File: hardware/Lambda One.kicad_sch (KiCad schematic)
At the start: 7 parts, among them IC1 01, J1 Conn_01x02, SW1 SW_Push, U1 W65C816SxP, U3 ATF22V10C, Y1 TFT680

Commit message: Added Board Register
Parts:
- removed R1: 4.7k, symbol Device:R_Small
- added C1, C20: 1uF, Capacitor_SMD:C_0603_1608Metric, symbol Device:C_Small
- added C21, C23, C25, C26, C27, C30, C4, C5: 100nF, Capacitor_SMD:C_0603_1608Metric, symbol Device:C_Small
- added L1: 120R @ 100MHz, Inductor_SMD:L_0603_1608Metric, symbol Device:L_Ferrite_Small
- added R17: 4.7k, Resistor_SMD:R_0603_1608Metric, symbol Device:R_Small_US
- added TP13: TestPoint_Small, TestPoint:TestPoint_Pad_D1.5mm, symbol Connector:TestPoint_Small
- added U6: 74AHC1G04, Package_TO_SOT_SMD:SOT-23-5, symbol 74xGxx:74AHC1G04
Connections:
- net +5V: now also U3.24 (VCC), R17.2
- net GND: now also C1.2, C20.2, C21.2, C23.2, C25.2, C26.2, C27.2, C30.2, C4.2, C5.2, U6.3 (GND)
- net IRQ_{1}: now also R17.1
- net R/~{W}: now also U6.2
- net BANK_{CS} renamed BoardReg_{~{CS}}
- new net +3.3V: C1.1, C4.1, C5.1, L1.1, U6.5 (VCC)
- new net +3.3VA: C20.1, C21.1, C23.1, C25.1, C26.1, C27.1, C30.1, L1.2, TP13.1
- new net ~{R}/W: U6.4
- no-connect marks 17 -> 16
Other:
- moved on the sheet: IC1, J1, SW1, U1, U3, Y1

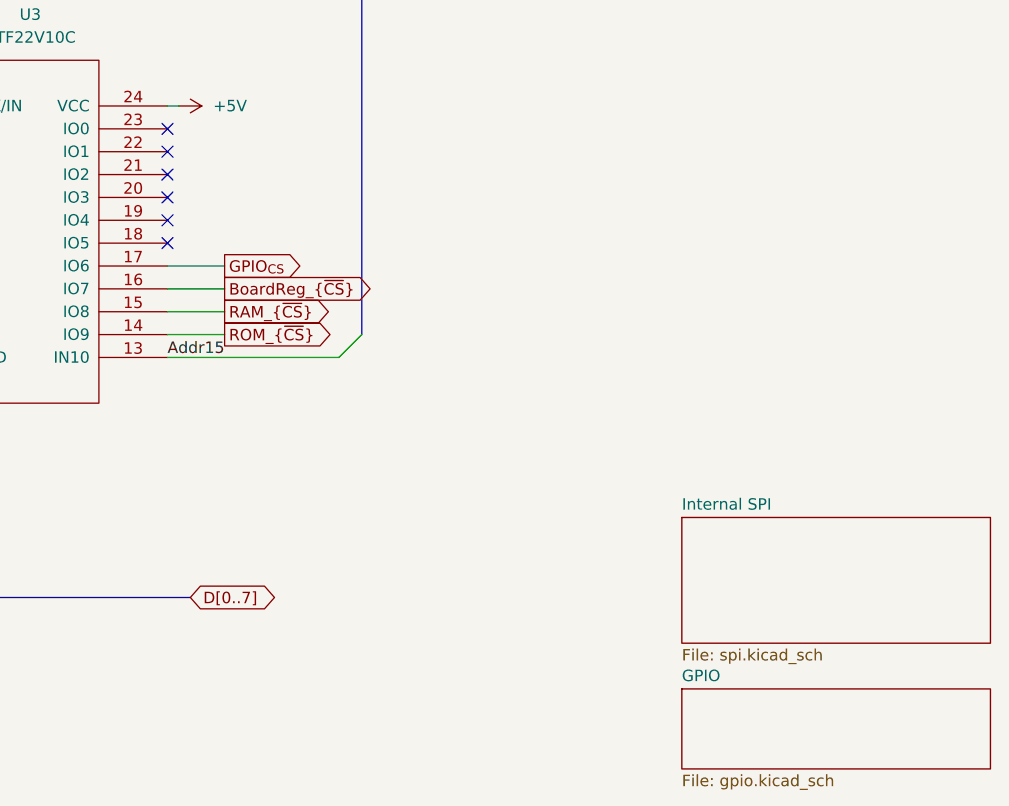
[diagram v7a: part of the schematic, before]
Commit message: Added External connectors
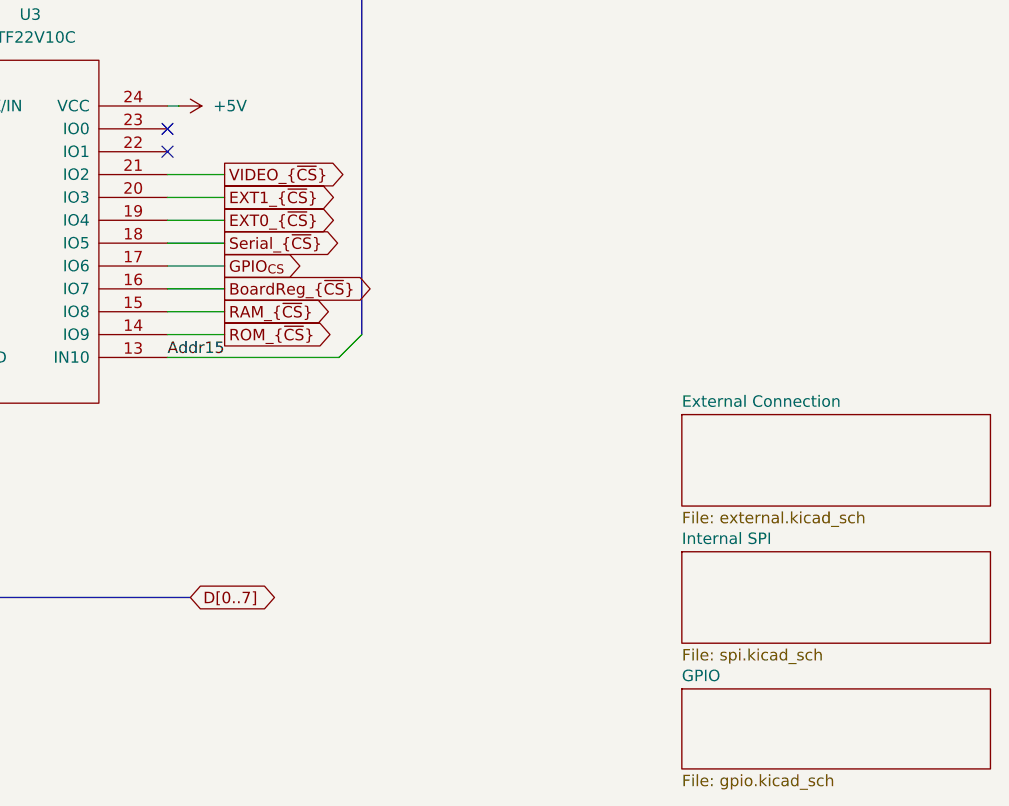
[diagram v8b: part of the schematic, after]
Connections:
- net Serial_{~{CS}}: now reaches U3.18 (IO5)
- net EXT0_{~{CS}}: now reaches U3.19 (IO4)
- net EXT1_{~{CS}}: now reaches U3.20 (IO3)
- net VIDEO_{~{CS}}: now reaches U3.21 (IO2)
- no-connect marks 16 -> 12
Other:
- added sheet External Connection (external.kicad_sch)
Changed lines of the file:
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@@
 	)
 	(no_connect
-		(at 190.5 81.28)
-	)
-	(no_connect
-		(at 190.5 86.36)
-	)
-	(no_connect
 		(at 106.68 88.9)
 	)
@@
 	)
 	(no_connect
-		(at 190.5 88.9)
-	)
-	(no_connect
-		(at 190.5 83.82)
-	)
-	(no_connect
 		(at 190.5 78.74)
 	)
@@
 		)
 	)
+	(wire
+		(pts
+			(xy 190.5 86.36) (xy 196.85 86.36)
+		)
+		(stroke
+			(width 0)
+			(type default)
+		)
+	)
 	(bus
 		(pts
@@
 		)
 	)
+	(wire
+		(pts
+			(xy 190.5 81.28) (xy 196.85 81.28)
+		)
+		(stroke
+			(width 0)
+			(type default)
+		)
+	)
 	(bus
 		(pts
@@
 		)
 	)
+	(wire
+		(pts
+			(xy 190.5 83.82) (xy 196.85 83.82)
+		)
+		(stroke
+			(width 0)
+			(type default)
+		)
+	)
 	(bus
 		(pts
@@
 	(wire
 		(pts
+			(xy 190.5 88.9) (xy 196.85 88.9)
+		)
+		(stroke
+			(width 0)
+			(type default)
+		)
+	)
+	(wire
+		(pts
 			(xy 127 76.2) (xy 135.89 76.2)
 		)
@@
 		)
 	)
+	(global_label "VIDEO_{~{CS}}"
+		(shape output)
+		(at 196.85 81.28 0)
+		(fields_autoplaced yes)
+		(effects
+			(font
+				(size 1.27 1.27)
+			)
+			(justify left)
+		)
+		(property "Intersheetrefs" "${INTERSHEET_REFS}"
+			(at 207.3125 81.28 0)
+			(effects
+				(font
+					(size 1.27 1.27)
+				)
+				(justify left)
+				(hide yes)
+			)
+		)
+	)
 	(global_label "CLK"
 		(shape output)
@@
 		)
 	)
+	(global_label "Serial_{~{CS}}"
+		(shape output)
+		(at 196.85 88.9 0)
+		(fields_autoplaced yes)
+		(effects
+			(font
+				(size 1.27 1.27)
+			)
+			(justify left)
+		)
+		(property "Intersheetrefs" "${INTERSHEET_REFS}"
+			(at 207.3729 88.9 0)
+			(effects
+				(font
+					(size 1.27 1.27)
+				)
+				(justify left)
+				(hide yes)
+			)
+		)
+	)
 	(global_label "~{R}{slash}W"
 		(shape output)
@@
 		)
 	)
+	(global_label "EXT1_{~{CS}}"
+		(shape output)
+		(at 196.85 83.82 0)
+		(fields_autoplaced yes)
+		(effects
+			(font
+				(size 1.27 1.27)
+			)
+			(justify left)
+		)
+		(property "Intersheetrefs" "${INTERSHEET_REFS}"
+			(at 206.4052 83.82 0)
+			(effects
+				(font
+					(size 1.27 1.27)
+				)
+				(justify left)
+				(hide yes)
+			)
+		)
+	)
 	(global_label "D[0..7]"
 		(shape bidirectional)
@@
 		)
 	)
+	(global_label "EXT0_{~{CS}}"
+		(shape output)
+		(at 196.85 86.36 0)
+		(fields_autoplaced yes)
+		(effects
+			(font
+				(size 1.27 1.27)
+			)
+			(justify left)
+		)
+		(property "Intersheetrefs" "${INTERSHEET_REFS}"
+			(at 206.4052 86.36 0)
+			(effects
+				(font
+					(size 1.27 1.27)
+				)
+				(justify left)
+				(hide yes)
+			)
+		)
+	)
 	(symbol
 		(lib_id "power:+5V")
@@
 	)
 	(sheet
-		(at 247.65 119.38)
-		(size 34.29 13.97)
+		(at 247.65 123.19)
+		(size 34.29 10.16)
 		(exclude_from_sim no)
 		(in_bom yes)
@@
 		)
 		(property "Sheetname" "Internal SPI"
-			(at 247.65 118.6684 0)
+			(at 247.65 122.4784 0)
 			(effects
 				(font
@@
 				)
 			)
+		)
+	)
+	(sheet
+		(at 247.65 107.95)
+		(size 34.29 10.16)
+		(exclude_from_sim no)
+		(in_bom yes)
+		(on_board yes)
+		(dnp no)
+		(fields_autoplaced yes)
+		(stroke
+			(width 0.1524)
+			(type solid)
+		)
+		(fill
+			(color 0 0 0 0.0000)
+		)
+		(property "Sheetname" "External Connection"
+			(at 247.65 107.2384 0)
+			(effects
+				(font
+					(size 1.27 1.27)
+				)
+				(justify left bottom)
+			)
+		)
+		(property "Sheetfile" "external.kicad_sch"
+			(at 247.65 118.6946 0)
+			(effects
+				(font
+					(size 1.27 1.27)
+				)
+				(justify left top)
+			)
+		)
+		(instances
+			(project "Lambda One"
+				(path "/73ea9964-373f-4fdc-b03e-f532cf836c0d"
+					(page "6")
+				)
+			)
